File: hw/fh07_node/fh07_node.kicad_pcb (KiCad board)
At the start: 4 copper layers, 35.4 x 19.4 mm, 35 parts, among them J1 Conn_ARM_JTAG_SWD_10, J2 Conn_01x02, M1 ME54BS01_V1.0, U1 BNO055

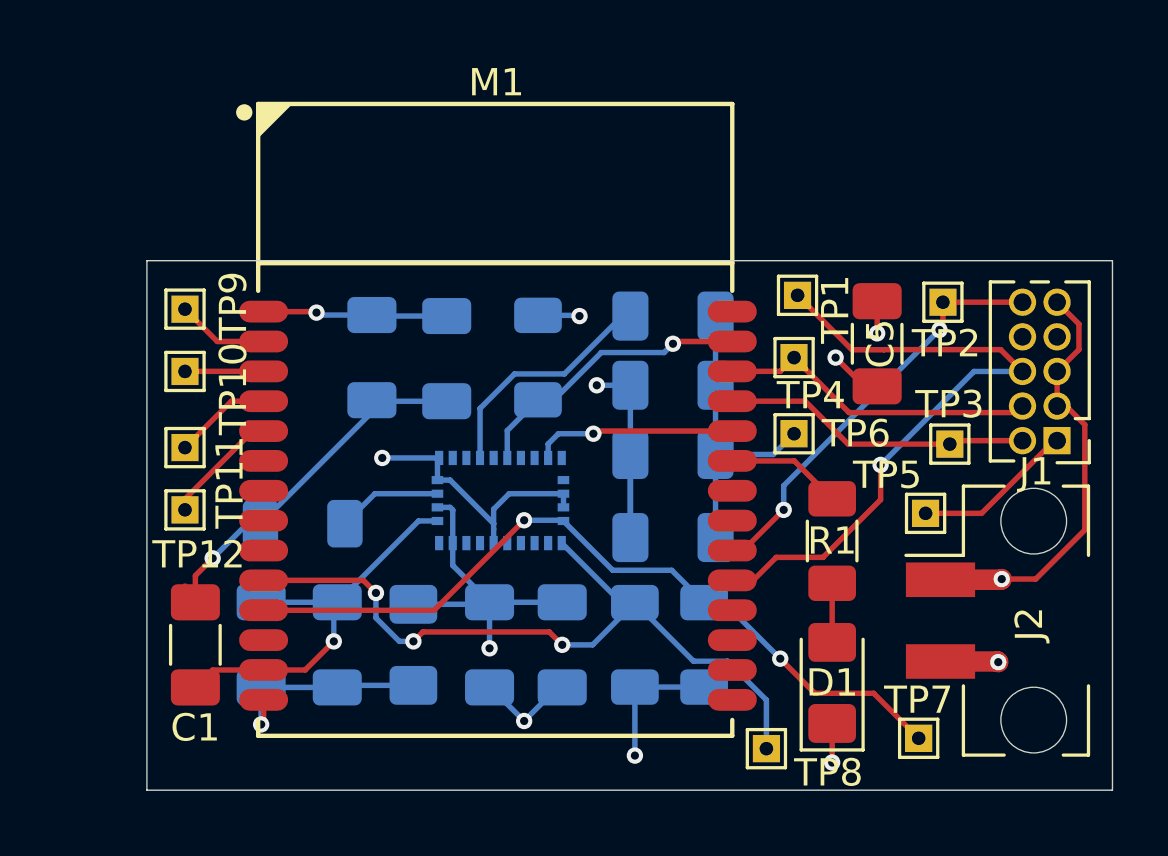
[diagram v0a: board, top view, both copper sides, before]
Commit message: Added rounded corners
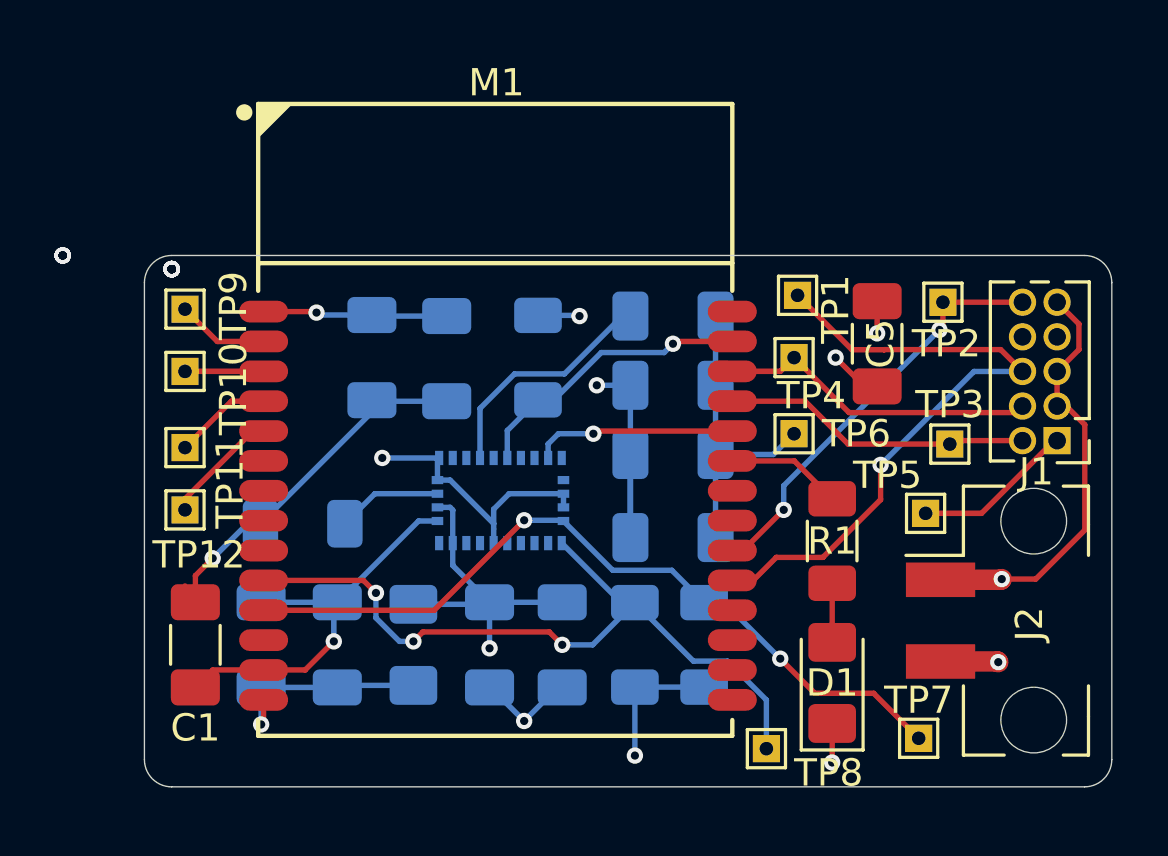
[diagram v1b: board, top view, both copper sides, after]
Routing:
- net (no net): vias 0 -> 25
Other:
- board size 35.4 x 19.4 mm -> 35.5 x 19.5 mm

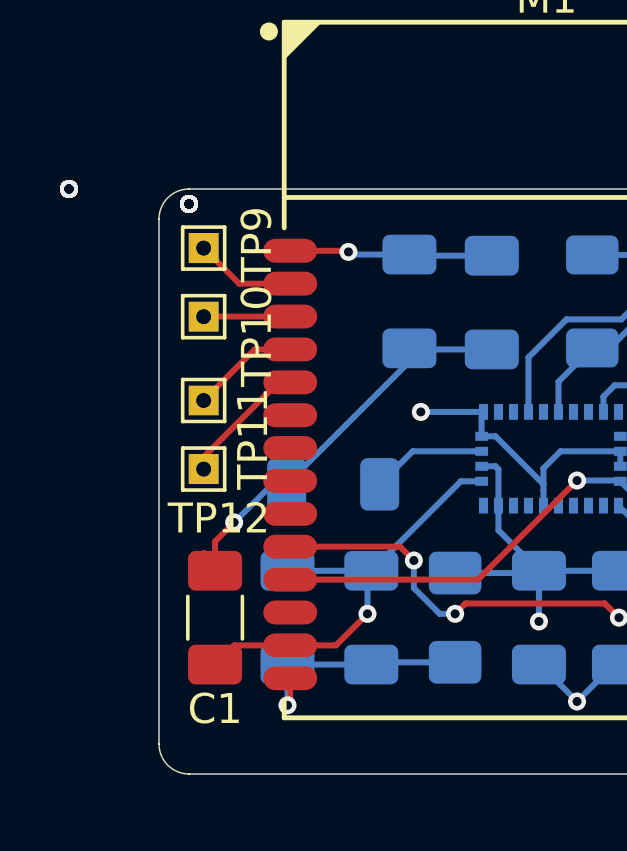
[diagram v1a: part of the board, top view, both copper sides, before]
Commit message: Added holes
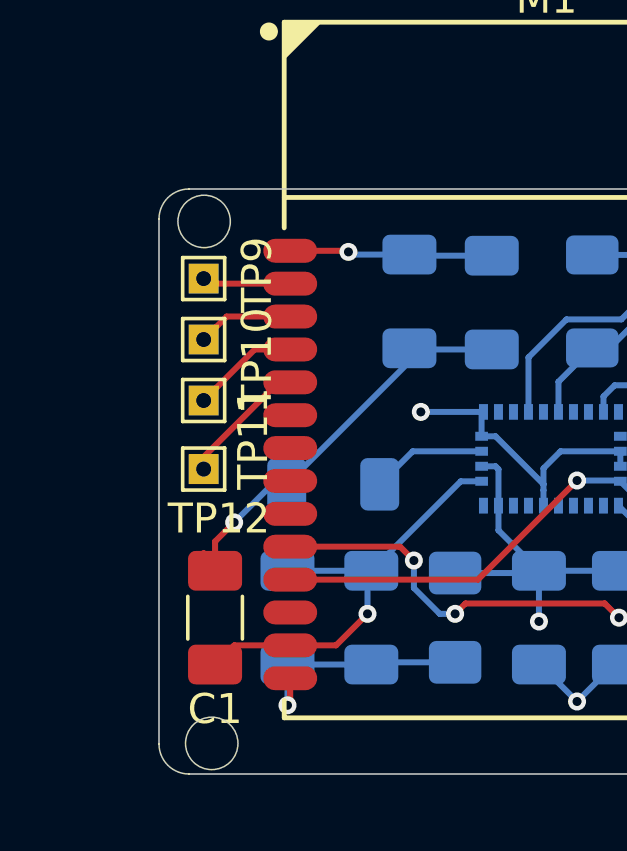
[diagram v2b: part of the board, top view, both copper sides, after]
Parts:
- moved TP9 1.02 mm to (102.5, 78.5)
- moved TP10 0.76 mm to (102.5, 80.5)
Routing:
- net (no net): vias 25 -> 0
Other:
- outline, holes or cut-outs redrawn
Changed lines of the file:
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@@
 	(footprint "TestPoint:TestPoint_THTPad_1.0x1.0mm_Drill0.5mm"
 		(layer "F.Cu")
-		(at 102.489 77.47)
+		(at 102.489 78.486)
 		(descr "THT rectangular pad as test Point, square 1.0mm side length, hole diameter 0.5mm")
 		(tags "test point THT pad rectangle square")
@@
 	(footprint "TestPoint:TestPoint_THTPad_1.0x1.0mm_Drill0.5mm"
 		(layer "F.Cu")
-		(at 102.489 79.756)
+		(at 102.489 80.518)
 		(descr "THT rectangular pad as test Point, square 1.0mm side length, hole diameter 0.5mm")
 		(tags "test point THT pad rectangle square")
@@
 		(layer "Edge.Cuts")
 	)
+	(gr_circle
+		(center 102.758237 93.98)
+		(end 101.888237 93.899)
+		(stroke
+			(width 0.05)
+			(type default)
+		)
+		(fill no)
+		(layer "Edge.Cuts")
+	)
 	(gr_line
 		(start 101 94)
@@
 		(layer "Edge.Cuts")
 	)
+	(gr_circle
+		(center 102.504237 76.581)
+		(end 101.634237 76.5)
+		(stroke
+			(width 0.05)
+			(type default)
+		)
+		(fill no)
+		(layer "Edge.Cuts")
+	)
 	(gr_arc
 		(start 136.5 94)
@@
 		(layer "Edge.Cuts")
 	)
-	(via
-		(at 102 76)
-		(size 0.6)
-		(drill 0.3)
-		(layers "F.Cu" "B.Cu")
-		(net 0)
-	)
-	(via
-		(at 102 76)
-		(size 0.6)
-		(drill 0.3)
-		(layers "F.Cu" "B.Cu")
-		(net 0)
-	)
-	(via
-		(at 102 76)
-		(size 0.6)
-		(drill 0.3)
-		(layers "F.Cu" "B.Cu")
-		(net 0)
-	)
-	(via
-		(at 102 76)
-		(size 0.6)
-		(drill 0.3)
-		(layers "F.Cu" "B.Cu")
-		(net 0)
-	)
-	(via
-		(at 102 76)
-		(size 0.6)
-		(drill 0.3)
-		(layers "F.Cu" "B.Cu")
-		(net 0)
-	)
-	(via
-		(at 102 76)
-		(size 0.6)
-		(drill 0.3)
-		(layers "F.Cu" "B.Cu")
-		(net 0)
-	)
-	(via
-		(at 102 76)
-		(size 0.6)
-		(drill 0.3)
-		(layers "F.Cu" "B.Cu")
-		(net 0)
-	)
-	(via
-		(at 102 76)
-		(size 0.6)
-		(drill 0.3)
-		(layers "F.Cu" "B.Cu")
-		(net 0)
-	)
-	(via
-		(at 102 76)
-		(size 0.6)
-		(drill 0.3)
-		(layers "F.Cu" "B.Cu")
-		(net 0)
-	)
-	(via
-		(at 98 75.5)
-		(size 0.6)
-		(drill 0.3)
-		(layers "F.Cu" "B.Cu")
-		(net 0)
-	)
-	(via
-		(at 98 75.5)
-		(size 0.6)
-		(drill 0.3)
-		(layers "F.Cu" "B.Cu")
-		(net 0)
-	)
-	(via
-		(at 102 76)
-		(size 0.6)
-		(drill 0.3)
-		(layers "F.Cu" "B.Cu")
-		(net 0)
-	)
-	(via
-		(at 102 76)
-		(size 0.6)
-		(drill 0.3)
-		(layers "F.Cu" "B.Cu")
-		(net 0)
-	)
-	(via
-		(at 102 76)
-		(size 0.6)
-		(drill 0.3)
-		(layers "F.Cu" "B.Cu")
-		(net 0)
-	)
-	(via
-		(at 98 75.5)
-		(size 0.6)
-		(drill 0.3)
-		(layers "F.Cu" "B.Cu")
-		(net 0)
-	)
-	(via
-		(at 102 76)
-		(size 0.6)
-		(drill 0.3)
-		(layers "F.Cu" "B.Cu")
-		(net 0)
-	)
-	(via
-		(at 102 76)
-		(size 0.6)
-		(drill 0.3)
-		(layers "F.Cu" "B.Cu")
-		(net 0)
-	)
-	(via
-		(at 102 76)
-		(size 0.6)
-		(drill 0.3)
-		(layers "F.Cu" "B.Cu")
-		(net 0)
-	)
-	(via
-		(at 102 76)
-		(size 0.6)
-		(drill 0.3)
-		(layers "F.Cu" "B.Cu")
-		(net 0)
-	)
-	(via
-		(at 98 75.5)
-		(size 0.6)
-		(drill 0.3)
-		(layers "F.Cu" "B.Cu")
-		(net 0)
-	)
-	(via
-		(at 102 76)
-		(size 0.6)
-		(drill 0.3)
-		(layers "F.Cu" "B.Cu")
-		(net 0)
-	)
-	(via
-		(at 102 76)
-		(size 0.6)
-		(drill 0.3)
-		(layers "F.Cu" "B.Cu")
-		(net 0)
-	)
-	(via
-		(at 102 76)
-		(size 0.6)
-		(drill 0.3)
-		(layers "F.Cu" "B.Cu")
-		(net 0)
-	)
-	(via
-		(at 102 76)
-		(size 0.6)
-		(drill 0.3)
-		(layers "F.Cu" "B.Cu")
-		(net 0)
-	)
-	(via
-		(at 98 75.5)
-		(size 0.6)
-		(drill 0.3)
-		(layers "F.Cu" "B.Cu")
-		(net 0)
-	)
 	(segment
 		(start 124.46 84.836)
@@
 	)
 	(segment
-		(start 105.37397 79.752)
-		(end 102.493 79.752)
+		(start 102.489 80.518)
+		(end 103.255 79.752)
 		(width 0.2)
 		(layer "F.Cu")
@@
 	)
 	(segment
-		(start 102.493 79.752)
-		(end 102.489 79.756)
+		(start 103.255 79.752)
+		(end 105.37397 79.752)
 		(width 0.2)
 		(layer "F.Cu")
@@
 	)
 	(segment
-		(start 105.37397 78.656)
-		(end 103.675 78.656)
+		(start 102.659 78.656)
+		(end 102.489 78.486)
 		(width 0.2)
 		(layer "F.Cu")
@@
 	)
 	(segment
-		(start 103.675 78.656)
-		(end 102.489 77.47)
+		(start 105.37397 78.656)
+		(end 102.659 78.656)
 		(width 0.2)
 		(layer "F.Cu")
